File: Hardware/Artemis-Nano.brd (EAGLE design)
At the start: 43.2 x 20.3 mm, 125 parts, among them J10 USB-C, J11 CORTEX_DEBUG, U1 ARTEMIS_MODULESMD, U2 MCP73831, U3 3.3V, U6 CH340E_MSOP10, Y2 32.768kHz

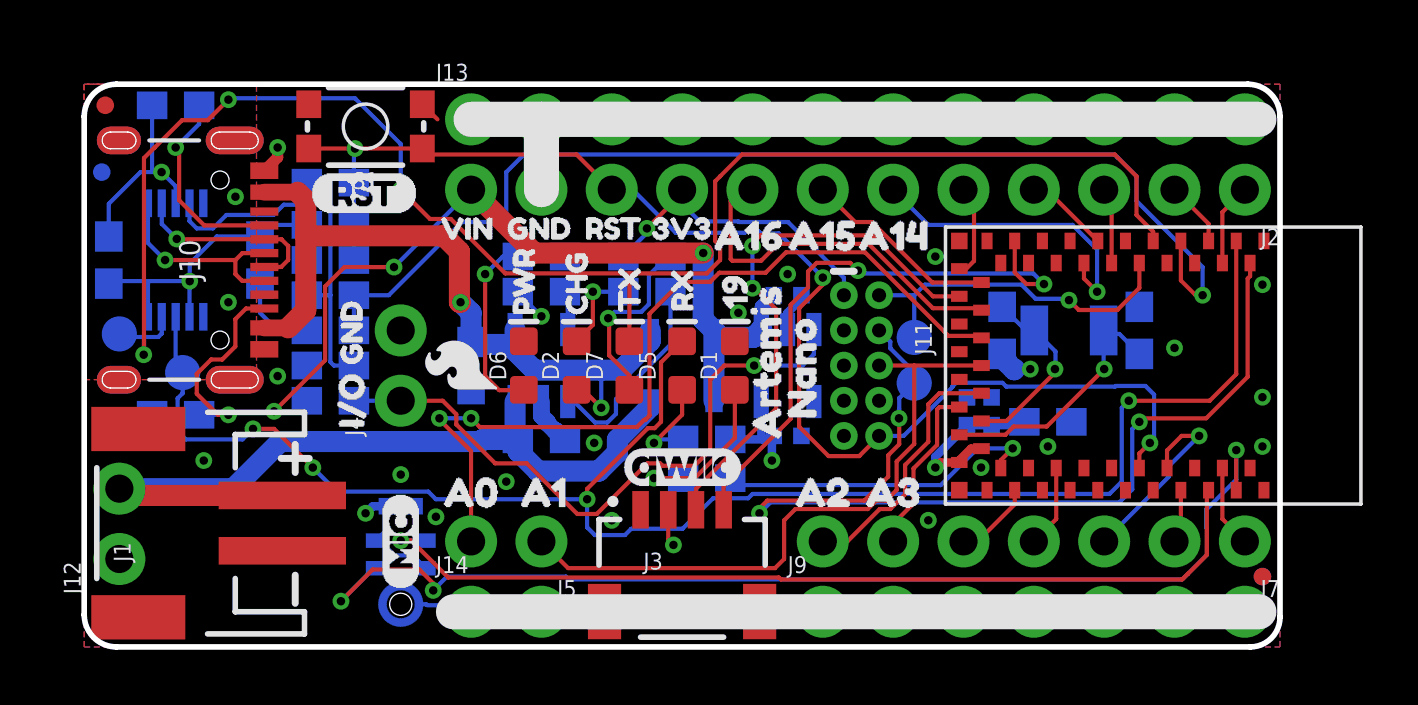
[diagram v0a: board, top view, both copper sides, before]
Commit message: Modify BL reset circuit to work with POR, SBL, and SVL
RTS doesn't like a 10k pull down. Remove R17. Increased R15 to 220k and reduced C21 to 0.1uF to maintain same RC time constant. Works for POR, SBL, and SVL.
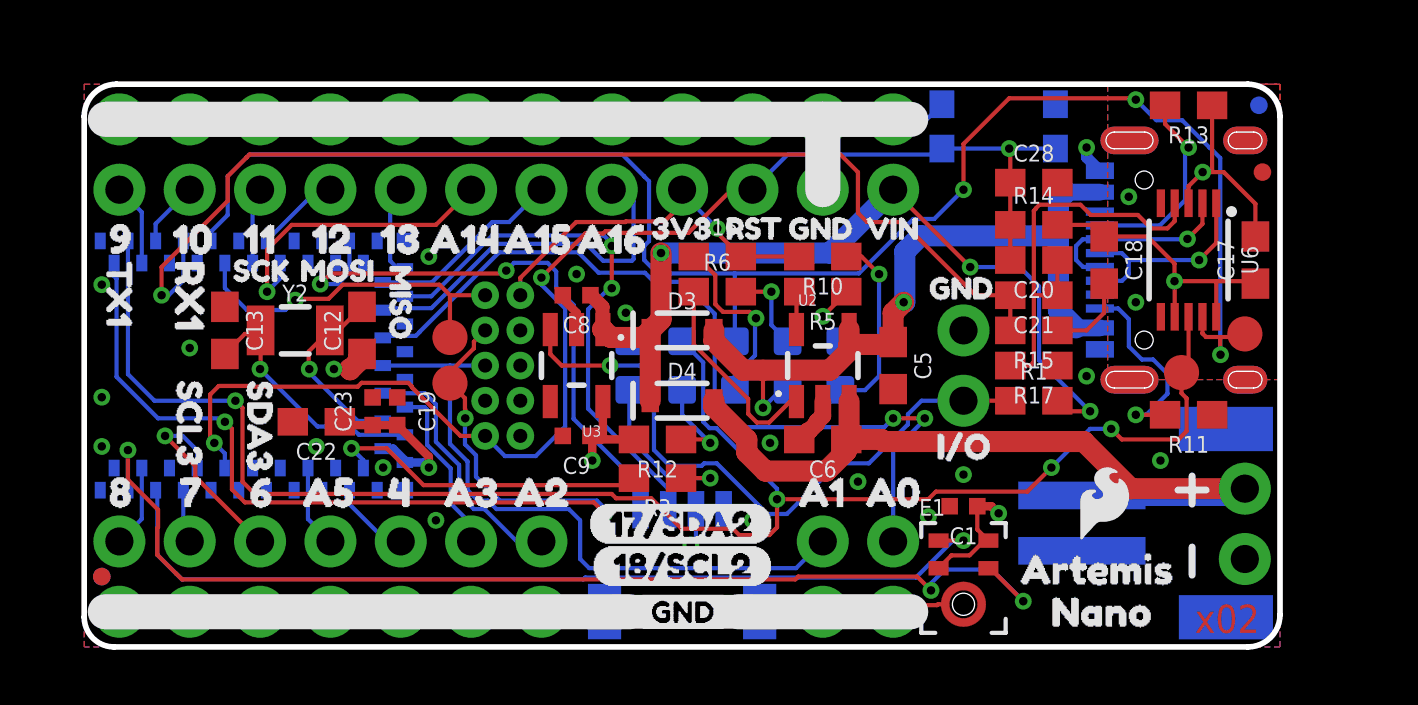
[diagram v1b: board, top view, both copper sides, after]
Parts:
- C21: value 2.2uF -> 0.1uF
- R15: value 22k -> 220k
- moved U$25 55.9 mm to (-6.35, 50.8), flipped to the bottom
- moved FRAME2 43.2 mm to (43.2, 0.00), flipped to the top
- moved U$37 43.2 mm to (0.00, 5.59), flipped to the top
- moved U$45 43.2 mm to (0.00, 14.7), flipped to the top
- moved FD1 41.9 mm to (0.64, 2.54), flipped to the bottom
- moved FD3 41.9 mm to (42.5, 17.1), flipped to the top
- moved FD4 41.9 mm to (0.64, 2.54), flipped to the top
- moved FD2 41.7 mm to (42.4, 19.6), flipped to the bottom
- moved C17 41.4 mm to (42.3, 14.0), flipped to the top
- moved J12 40.6 mm to (41.9, 3.17), flipped to the bottom
- moved J2 40.6 mm to (1.27, 16.5), flipped to the bottom
- moved J7 40.6 mm to (1.27, 3.81), flipped to the bottom
- moved TP6 40.6 mm to (41.9, 11.3), flipped to the top
- moved U$59 40.6 mm to (1.27, 14.9), flipped to the top
- moved U$46 38.6 mm to (2.29, 14.7), flipped to the top
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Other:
- outline, holes or cut-outs redrawn
